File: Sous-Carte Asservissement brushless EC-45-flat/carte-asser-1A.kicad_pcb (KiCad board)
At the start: 2 copper layers, 60 x 60 mm, 58 parts, among them K1 Maxon-200142, K2 Maxon-200142, P1 swdio, P2 CAN bus, P3 usb, P4 serial bus, P5 5V, P6 8..24V, P7 encoder 1, P8 encoder 2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

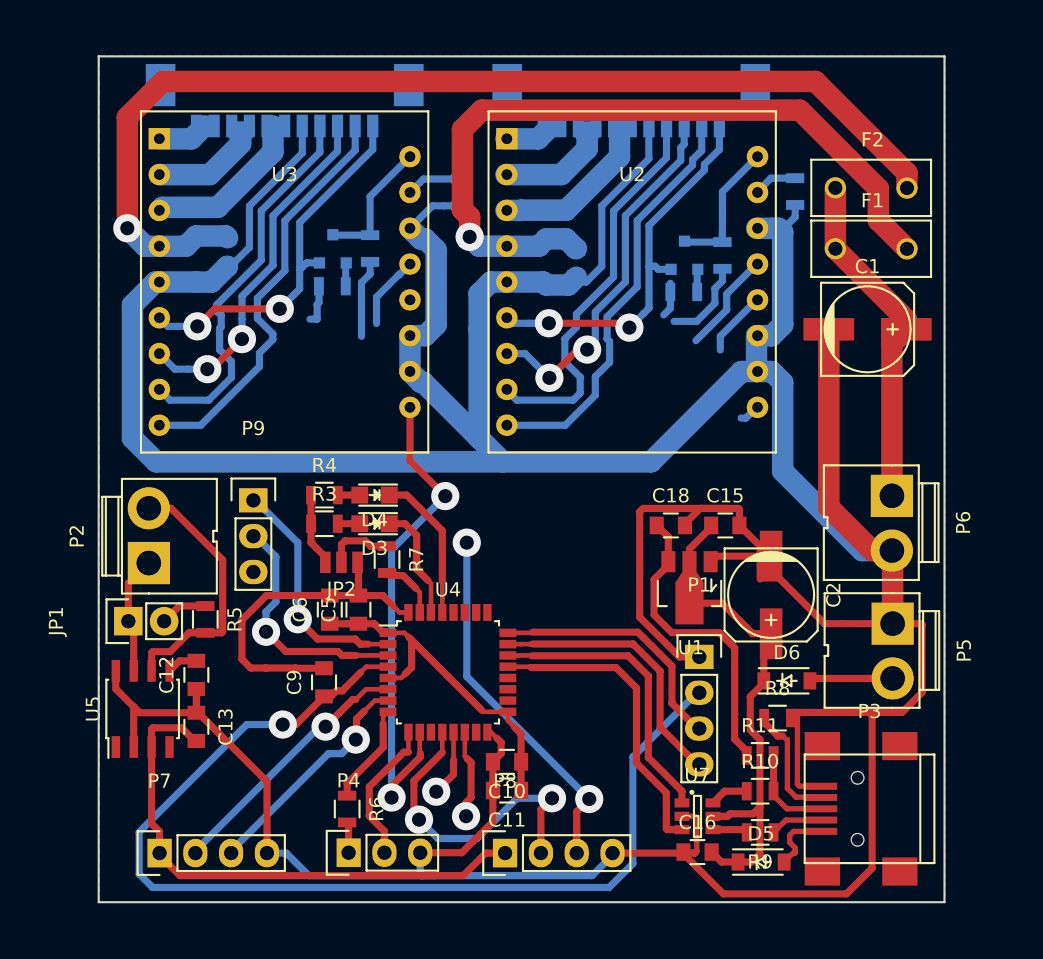
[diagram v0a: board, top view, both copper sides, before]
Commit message: asser 1A : routé
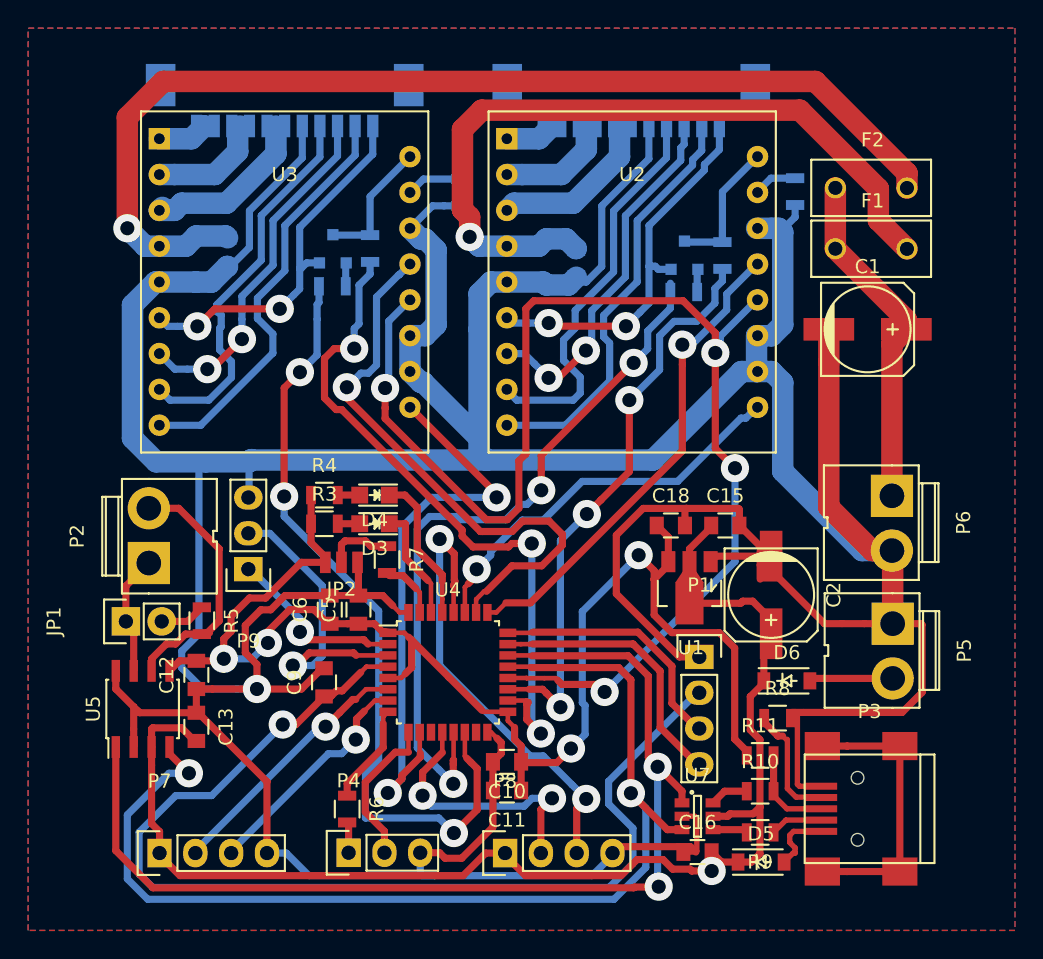
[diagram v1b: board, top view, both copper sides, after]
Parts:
- moved P9 4.89 mm to (35.4, 64.3), turned to 180 degrees
- moved R5 0.27 mm to (32.1, 67.9)
- moved JP1 0.17 mm to (26.8, 68.0)
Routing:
- net /uC-part/gpio_enable: track 4.62 -> 93.1 mm, vias 0 -> 4
- net /uC-part/can_rx: track 21.7 -> 78.4 mm, vias 0 -> 2
- net /uC-part/can_tx: track 20.6 -> 76.1 mm, vias 0 -> 2
- net /uC-part/pwm2_neg: track 9.31 -> 56.9 mm, vias 1 -> 3
- net +3V3: track 54.3 -> 100.0 mm, vias 0 -> 4
- net /uC-part/pwm1_neg: track 7.18 -> 51.4 mm, vias 1 -> 3
- net /uC-part/pwm2_pos: track 5.54 -> 49.2 mm, vias 0 -> 3
- net /uC-part/gpio_direction2: track 5.22 -> 41.0 mm, vias 0 -> 1
- net /uC-part/pwm1_pos: track 6.09 -> 41.1 mm, vias 0 -> 3
- net /uC-part/gpio_direction1: track 7.21 -> 34.4 mm, vias 0 -> 1
- net /uC-part/gpio_ready1: track 1.42 -> 28.2 mm, vias 0 -> 1
- net +5V: track 72.7 -> 95.0 mm, vias 0 -> 1
- net Net-(P3-Pad6): track 0.00 -> 19.9 mm
- net /encoder-part/encoder2_2: track 26.0 -> 33.2 mm
- net /uC-part/gpio_ready2: track 35.8 -> 41.1 mm
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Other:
- board outline removed

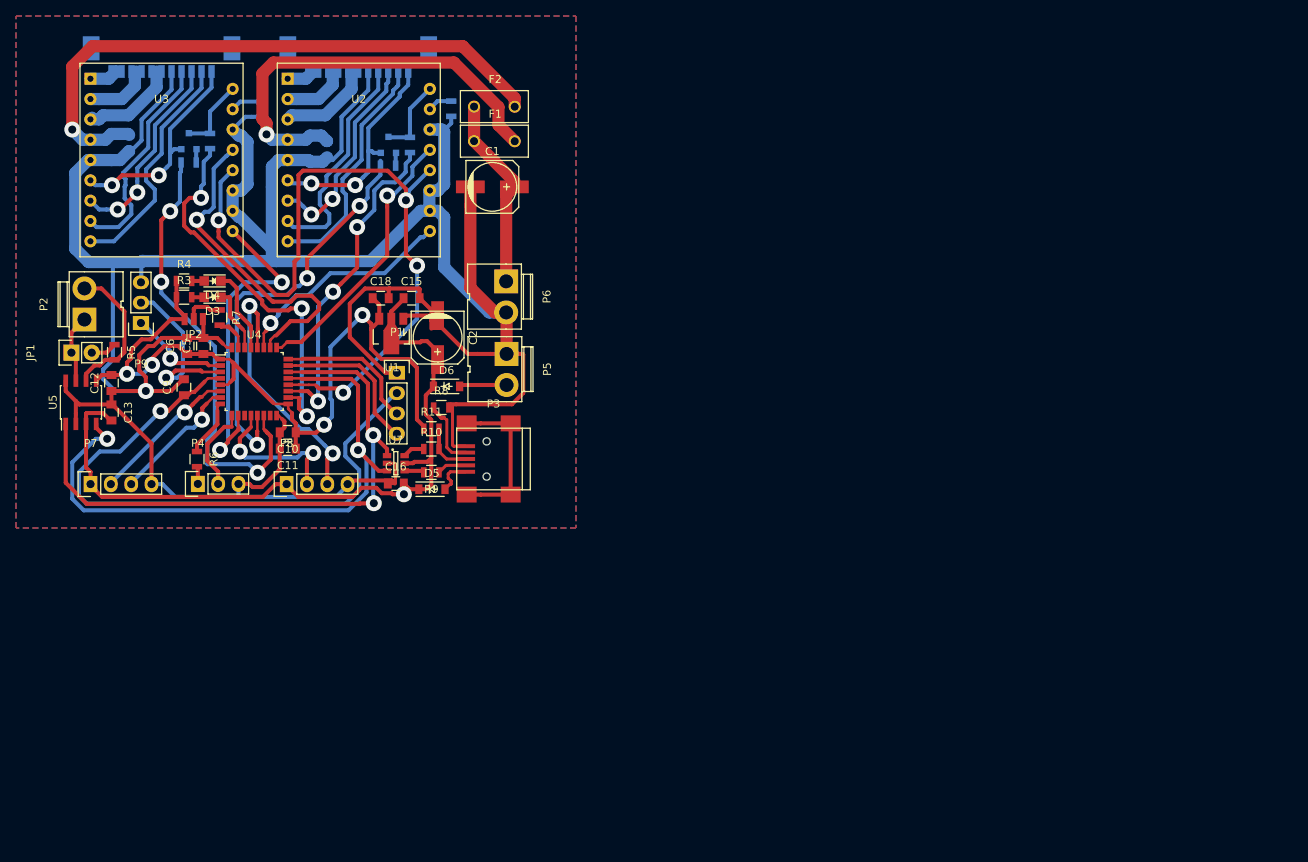
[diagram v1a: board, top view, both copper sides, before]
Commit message: asser 1A : corrections sur le  routage + trous visses
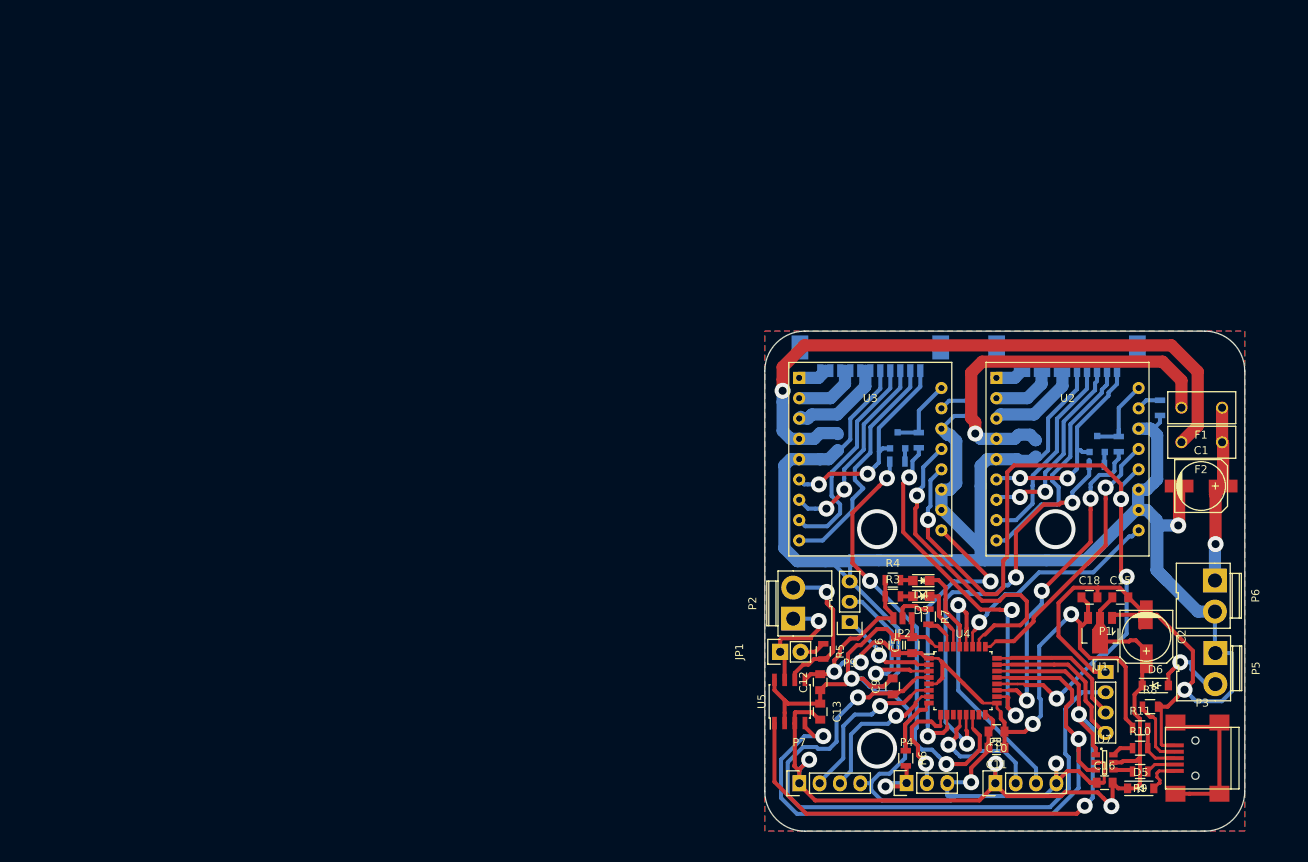
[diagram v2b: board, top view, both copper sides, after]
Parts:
- moved F2 97.9 mm to (168.1, 79.2), turned to 180 degrees
- moved D4 96.2 mm to (133.0, 96.5)
- moved R12 96.2 mm to (154.9, 82.0)
- moved C1 96.2 mm to (168.0, 84.6)
- moved C10 96.2 mm to (142.4, 115.3)
- moved C11 96.2 mm to (142.4, 117.4)
- moved C12 96.2 mm to (120.4, 109.2)
- moved C13 96.2 mm to (120.4, 112.8)
- moved C16 96.2 mm to (155.9, 121.7)
- moved C18 96.2 mm to (154.0, 98.6)
- moved C2 96.2 mm to (161.1, 103.5)
- moved C3 96.2 mm to (147.3, 79.9)
- moved C4 96.2 mm to (122.6, 79.1)
- moved C5 96.2 mm to (131.9, 104.5)
- moved C6 96.2 mm to (129.8, 104.5)
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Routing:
- net GND: track 403.3 -> 424.8 mm, vias 1 -> 5
- net +5V: track 95.0 -> 109.4 mm, vias 1 -> 3
- net Net-(JP1-Pad1): track 9.09 -> 15.6 mm, vias 0 -> 1
- net /brushless-part/power1: track 53.7 -> 47.5 mm
- net Net-(P4-Pad1): track 2.19 -> 7.80 mm, vias 0 -> 1
- net /uC-part/can_tx: track 76.1 -> 81.3 mm
- net /uC-part/can_rx: track 78.4 -> 82.5 mm
- net Net-(D6-Pad2): track 5.94 -> 9.82 mm, vias 0 -> 1
- net /brushless-part/power2: track 76.0 -> 79.7 mm
- net /uC-part/nrst: track 77.6 -> 81.3 mm
- net Net-(K1-Pad8): track 28.3 -> 24.9 mm
- net /encoder-part/encoder1_2: track 16.5 -> 19.4 mm
- net /uC-part/gpio_enable: track 93.1 -> 96.0 mm
- net /encoder-part/encoder1_1: track 18.6 -> 20.9 mm
- net /serial-part/tx: track 11.0 -> 13.4 mm, vias 0 -> 1
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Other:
- board outline added: 60 x 62.5 mm

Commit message: asser 1A : removed serial tx protection resistor, leaves some space for the screw's head
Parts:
- removed R6: 1k, Resistors_SMD:R_0805
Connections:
- P4 pad 1: Net-(P4-Pad1) -> /serial-part/rx
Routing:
- net /serial-part/rx: track 7.68 -> 17.4 mm, vias 0 -> 1
- net Net-(P4-Pad1): track 7.80 -> 0.00 mm, vias 1 -> 0
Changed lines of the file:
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@@
 (kicad_pcb (version 4) (host pcbnew 0.201604021231+6659~43~ubuntu15.10.1-product)
   (general
-    (links 157)
-    (no_connects 0)
+    (links 156)
+    (no_connects 1)
     (area 113.351239 65.202999 173.501241 127.853001)
     (thickness 1)
     (drawings 10)
-    (tracks 1050)
+    (tracks 1048)
     (zones 0)
-    (modules 58)
-    (nets 69)
+    (modules 57)
+    (nets 68)
   )
   (page A4)
@@
   (net 63 +5V_weak2)
   (net 64 +5V_weak1)
-  (net 65 "Net-(P4-Pad1)")
-  (net 66 /serial-part/tx)
-  (net 67 "Net-(U4-Pad15)")
-  (net 68 "Net-(U4-Pad11)")
+  (net 65 /serial-part/tx)
+  (net 66 "Net-(U4-Pad15)")
+  (net 67 "Net-(U4-Pad11)")
   (net_class Default "This is the default net class."
     (clearance 0.3302)
@@
     (add_net "Net-(P3-Pad4)")
     (add_net "Net-(P3-Pad6)")
-    (add_net "Net-(P4-Pad1)")
     (add_net "Net-(Q1-Pad1)")
     (add_net "Net-(Q2-Pad1)")
@@
   )
   (module Resistors_SMD:R_0805 (layer F.Cu)
-    (at 131.05384 118.6688 270)
-    (descr "Resistor SMD 0805, reflow soldering, Vishay (see dcrcw.pdf)")
-    (tags "resistor 0805")
-    (attr smd)
-    (fp_text reference R6 (at 0 -2.1 270) (layer F.SilkS)
-      (effects (font (size 1 1) (thickness 0.15)))
-    )
-    (fp_text value 1k (at 0 2.1 270) (layer F.Fab)
-      (effects (font (size 1 1) (thickness 0.15)))
-    )
-    (fp_line (start -1.6 -1) (end 1.6 -1) (layer F.CrtYd) (width 0.05))
-    (fp_line (start -1.6 1) (end 1.6 1) (layer F.CrtYd) (width 0.05))
-    (fp_line (start -1.6 -1) (end -1.6 1) (layer F.CrtYd) (width 0.05))
-    (fp_line (start 1.6 -1) (end 1.6 1) (layer F.CrtYd) (width 0.05))
-    (fp_line (start 0.6 0.875) (end -0.6 0.875) (layer F.SilkS) (width 0.15))
-    (fp_line (start -0.6 -0.875) (end 0.6 -0.875) (layer F.SilkS) (width 0.15))
-    (pad 1 smd rect (at -0.95 0 270) (size 0.7 1.3) (layers F.Cu F.Paste F.Mask)
-      (net 27 /serial-part/rx))
-    (pad 2 smd rect (at 0.95 0 270) (size 0.7 1.3) (layers F.Cu F.Paste F.Mask)
-      (net 65 "Net-(P4-Pad1)"))
-    (model Resistors_SMD.3dshapes/R_0805.wrl
-      (at (xyz 0 0 0))
-      (scale (xyz 1 1 1))
-      (rotate (xyz 0 0 0))
-    )
-  )
-  (module Resistors_SMD:R_0805 (layer F.Cu)
     (at 133.8834 100.97008 270)
     (descr "Resistor SMD 0805, reflow soldering, Vishay (see dcrcw.pdf)")
@@
     (fp_line (start 1.27 1.27) (end 1.27 -1.27) (layer F.SilkS) (width 0.15))
     (pad 1 thru_hole rect (at 0 0) (size 1.7272 2.032) (drill 1.016) (layers *.Cu *.Mask F.SilkS)
-      (net 65 "Net-(P4-Pad1)"))
+      (net 27 /serial-part/rx))
     (pad 2 thru_hole oval (at 2.54 0) (size 1.7272 2.032) (drill 1.016) (layers *.Cu *.Mask F.SilkS)
-      (net 66 /serial-part/tx))
+      (net 65 /serial-part/tx))
     (pad 3 thru_hole oval (at 5.08 0) (size 1.7272 2.032) (drill 1.016) (layers *.Cu *.Mask F.SilkS)
       (net 3 GND))
@@
       (net 27 /serial-part/rx))
     (pad 9 smd rect (at -2.8 4.25 90) (size 1.2 0.6) (layers F.Cu F.Paste F.Mask)
-      (net 66 /serial-part/tx))
+      (net 65 /serial-part/tx))
     (pad 10 smd rect (at -2 4.25 90) (size 1.2 0.6) (layers F.Cu F.Paste F.Mask)
       (net 10 /uC-part/gpio_ready2))
     (pad 11 smd rect (at -1.2 4.25 90) (size 1.2 0.6) (layers F.Cu F.Paste F.Mask)
-      (net 68 "Net-(U4-Pad11)"))
+      (net 67 "Net-(U4-Pad11)"))
     (pad 12 smd rect (at -0.4 4.25 90) (size 1.2 0.6) (layers F.Cu F.Paste F.Mask)
       (net 61 /encoder-part/encoder2_1))
@@
       (net 42 /uC-part/pwm2_neg))
     (pad 15 smd rect (at 2 4.25 90) (size 1.2 0.6) (layers F.Cu F.Paste F.Mask)
-      (net 67 "Net-(U4-Pad15)"))
+      (net 66 "Net-(U4-Pad15)"))
     (pad 16 smd rect (at 2.8 4.25 90) (size 1.2 0.6) (layers F.Cu F.Paste F.Mask)
       (net 3 GND))
@@
   (segment (start 131.8514 105.52608) (end 132.9844 105.52608) (width 0.508) (layer F.Cu) (net 26))
   (segment (start 132.9844 105.52608) (end 133.570199 106.111879) (width 0.508) (layer F.Cu) (net 26))
+  (segment (start 130.96855 116.77551) (end 131.15544 116.9624) (width 0.508) (layer F.Cu) (net 27))
+  (segment (start 131.15544 116.9624) (end 131.15544 121.7676) (width 0.508) (layer F.Cu) (net 27))
   (segment (start 130.96855 114.463362) (end 130.96855 116.77551) (width 0.508) (layer F.Cu) (net 27))
   (segment (start 132.821352 112.61056) (end 130.96855 114.463362) (width 0.508) (layer F.Cu) (net 27))
-  (segment (start 131.05384 116.8608) (end 131.05384 117.7188) (width 0.508) (layer F.Cu) (net 27))
-  (segment (start 130.96855 116.77551) (end 131.05384 116.8608) (width 0.508) (layer F.Cu) (net 27))
   (segment (start 133.60688 112.61056) (end 132.821352 112.61056) (width 0.508) (layer F.Cu) (net 27))
   (segment (start 133.60688 112.1156) (end 133.60688 112.61056) (width 0.3302) (layer F.Cu) (net 27))
   (segment (start 133.9514 111.77108) (end 133.60688 112.1156) (width 0.3302) (layer F.Cu) (net 27))
+  (segment (start 128.524 122.18416) (end 130.73888 122.18416) (width 0.508) (layer F.Cu) (net 27))
+  (segment (start 130.73888 122.18416) (end 131.15544 121.7676) (width 0.508) (layer F.Cu) (net 27))
+  (via (at 128.524 122.18416) (size 2) (drill 1) (layers F.Cu B.Cu) (net 27))
+  (segment (start 131.15544 121.7676) (end 128.94056 121.7676) (width 0.508) (layer B.Cu) (net 27))
+  (segment (start 128.94056 121.7676) (end 128.524 122.18416) (width 0.508) (layer B.Cu) (net 27))
   (segment (start 159.4002 117.40388) (end 157.8332 117.40388) (width 0.508) (layer F.Cu) (net 28))
   (segment (start 157.8332 117.40388) (end 157.0052 118.23188) (width 0.508) (layer F.Cu) (net 28))
@@
   (segment (start 154.03064 80.38338) (end 153.12259 80.38338) (width 0.508) (layer B.Cu) (net 64))
   (segment (start 157.4562 70.21508) (end 157.4562 71.88782) (width 0.508) (layer B.Cu) (net 64))
-  (segment (start 128.524 122.18416) (end 130.73888 122.18416) (width 0.508) (layer F.Cu) (net 65))
-  (segment (start 130.73888 122.18416) (end 131.15544 121.7676) (width 0.508) (layer F.Cu) (net 65))
-  (via (at 128.524 122.18416) (size 2) (drill 1) (layers F.Cu B.Cu) (net 65))
-  (segment (start 131.15544 121.7676) (end 128.94056 121.7676) (width 0.508) (layer B.Cu) (net 65))
-  (segment (start 128.94056 121.7676) (end 128.524 122.18416) (width 0.508) (layer B.Cu) (net 65))
-  (segment (start 131.15544 121.7676) (end 131.15544 119.7204) (width 0.508) (layer F.Cu) (net 65))
-  (segment (start 131.15544 119.7204) (end 131.05384 119.6188) (width 0.508) (layer F.Cu) (net 65))
-  (segment (start 134.24916 114.07648) (end 132.540841 114.07648) (width 0.508) (layer F.Cu) (net 66))
-  (segment (start 132.540841 114.07648) (end 131.806761 114.81056) (width 0.508) (layer F.Cu) (net 66))
-  (segment (start 134.80704 114.63436) (end 134.24916 114.07648) (width 0.508) (layer F.Cu) (net 66))
-  (segment (start 135.4014 114.63436) (end 134.80704 114.63436) (width 0.508) (layer F.Cu) (net 66))
-  (segment (start 131.806761 114.81056) (end 131.806761 116.331396) (width 0.508) (layer F.Cu) (net 66))
-  (segment (start 131.806761 116.331396) (end 132.575166 117.099801) (width 0.508) (layer F.Cu) (net 66))
-  (segment (start 132.575166 117.099801) (end 132.575166 118.31837) (width 0.508) (layer F.Cu) (net 66))
-  (segment (start 132.575166 118.31837) (end 133.575165 119.318369) (width 0.508) (layer F.Cu) (net 66))
-  (segment (start 133.69544 121.7676) (end 133.69544 119.438644) (width 0.508) (layer B.Cu) (net 66))
-  (segment (start 133.69544 119.438644) (end 133.575165 119.318369) (width 0.508) (layer B.Cu) (net 66))
-  (via (at 133.575165 119.318369) (size 2) (drill 1) (layers F.Cu B.Cu) (net 66))
-  (segment (start 133.69544 121.7676) (end 133.69544 121.6914) (width 0.508) (layer B.Cu) (net 66))
-  (segment (start 135.4014 113.22108) (end 135.4014 114.63436) (width 0.3302) (layer F.Cu) (net 66))
+  (segment (start 134.24916 114.07648) (end 132.540841 114.07648) (width 0.508) (layer F.Cu) (net 65))
+  (segment (start 132.540841 114.07648) (end 131.806761 114.81056) (width 0.508) (layer F.Cu) (net 65))
+  (segment (start 134.80704 114.63436) (end 134.24916 114.07648) (width 0.508) (layer F.Cu) (net 65))
+  (segment (start 135.4014 114.63436) (end 134.80704 114.63436) (width 0.508) (layer F.Cu) (net 65))
+  (segment (start 131.806761 114.81056) (end 131.806761 116.331396) (width 0.508) (layer F.Cu) (net 65))
+  (segment (start 131.806761 116.331396) (end 132.575166 117.099801) (width 0.508) (layer F.Cu) (net 65))
+  (segment (start 132.575166 117.099801) (end 132.575166 118.31837) (width 0.508) (layer F.Cu) (net 65))
+  (segment (start 132.575166 118.31837) (end 133.575165 119.318369) (width 0.508) (layer F.Cu) (net 65))
+  (segment (start 133.69544 121.7676) (end 133.69544 119.438644) (width 0.508) (layer B.Cu) (net 65))
+  (segment (start 133.69544 119.438644) (end 133.575165 119.318369) (width 0.508) (layer B.Cu) (net 65))
+  (via (at 133.575165 119.318369) (size 2) (drill 1) (layers F.Cu B.Cu) (net 65))
+  (segment (start 133.69544 121.7676) (end 133.69544 121.6914) (width 0.508) (layer B.Cu) (net 65))
+  (segment (start 135.4014 113.22108) (end 135.4014 114.63436) (width 0.3302) (layer F.Cu) (net 65))
   (zone (net 3) (net_name GND) (layer F.Cu) (hatch edge 0.508)
     (connect_pads (clearance 0.508))
